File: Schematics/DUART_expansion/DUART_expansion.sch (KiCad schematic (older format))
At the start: 11 parts

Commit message: Initial working version (still unstable!)
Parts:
- added unit 5 of U1
- added unit 6 of U1
- added unit 4 of U2
- U1: renamed from U?; value 74AHC04 -> 74HC04; symbol 74xx:74AHC04 -> 74xx:74HC04
- gave numbers to parts that had none: 4
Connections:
- net +5V: now also U1.14 (VCC), U2.14 (VCC); no longer U1.7 (GND), U2.7 (GND)
- net CLK: now also U2.13
- net DUART_CEN: now also U2.11; no longer U2.8
- net GND: now also U1.7 (GND), U2.7 (GND), U1.13; no longer U1.14 (VCC), U2.14 (VCC)
- net d6: no longer U3.21 (D7)
- net d7: now also U3.21 (D7)
- new net: U1.10, U2.12
- new net: U1.11, U2.8
- no-connect marks 20 -> 21
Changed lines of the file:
@@
 $EndDescr
 $Comp
-L Connector_Generic:Conn_02x16_Odd_Even J?
+L Connector_Generic:Conn_02x16_Odd_Even J1
 U 1 1 5F15BD0D
 P 1400 1650
-F 0 "J?" H 1450 2567 50  0000 C CNN
+F 0 "J1" H 1450 2567 50  0000 C CNN
 F 1 "Expansion bus" H 1450 2476 50  0000 C CNN
 F 2 "" H 1400 1650 50  0001 C CNN
@@
 	3550 1850 3550 1750
 $Comp
-L Oscillator:CXO_DIP8 X?
+L Oscillator:CXO_DIP8 X1
 U 1 1 5F1792E7
 P 3550 1450
-F 0 "X?" H 3894 1496 50  0000 L CNN
+F 0 "X1" H 3894 1496 50  0000 L CNN
 F 1 "CXO_DIP8" H 3894 1405 50  0000 L CNN
 F 2 "Oscillator:Oscillator_DIP-8" H 4000 1100 50  0001 C CNN
@@
 	3850 1450 4300 1450
 $Comp
-L 74xx:74AHC04 U?
+L 74xx:74HC04 U1
 U 7 1 5F17BEEB
 P 1100 3800
-F 0 "U?" H 1330 3846 50  0000 L CNN
-F 1 "74AHC04" H 1330 3755 50  0000 L CNN
+F 0 "U1" H 1330 3846 50  0000 L CNN
+F 1 "74HC04" H 1330 3755 50  0000 L CNN
 F 2 "" H 1100 3800 50  0001 C CNN
 F 3 "https://assets.nexperia.com/documents/data-sheet/74AHC_AHCT04.pdf" H 1100 3800 50  0001 C CNN
@@
 	1    0    0    -1
 $EndComp
-Text GLabel 1100 3200 1    50   Input ~ 0
-GND
 Wire Wire Line
 	1100 3200 1100 3300
-Text GLabel 1100 4400 3    50   Input ~ 0
-+5V
 Wire Wire Line
 	1100 4400 1100 4300
 $Comp
-L 74xx:74AHC04 U?
+L 74xx:74HC04 U1
 U 1 1 5F17F7FF
 P 3500 2700
-F 0 "U?" H 3500 3017 50  0000 C CNN
-F 1 "74AHC04" H 3500 2926 50  0000 C CNN
+F 0 "U1" H 3500 3017 50  0000 C CNN
+F 1 "74HC04" H 3500 2926 50  0000 C CNN
 F 2 "" H 3500 2700 50  0001 C CNN
 F 3 "https://assets.nexperia.com/documents/data-sheet/74AHC_AHCT04.pdf" H 3500 2700 50  0001 C CNN
@@
 	3800 2700 3900 2700
 $Comp
-L 74xx:74AHC04 U?
+L 74xx:74HC04 U1
 U 2 1 5F185D8B
 P 3500 3900
-F 0 "U?" H 3500 4217 50  0000 C CNN
-F 1 "74AHC04" H 3500 4126 50  0000 C CNN
+F 0 "U1" H 3500 4217 50  0000 C CNN
+F 1 "74HC04" H 3500 4126 50  0000 C CNN
 F 2 "" H 3500 3900 50  0001 C CNN
 F 3 "https://assets.nexperia.com/documents/data-sheet/74AHC_AHCT04.pdf" H 3500 3900 50  0001 C CNN
@@
 $EndComp
 $Comp
-L 74xx:74HC00 U?
+L 74xx:74HC00 U2
 U 1 1 5F187D21
 P 3500 3250
-F 0 "U?" H 3500 3575 50  0000 C CNN
+F 0 "U2" H 3500 3575 50  0000 C CNN
 F 1 "74HC00" H 3500 3484 50  0000 C CNN
 F 2 "" H 3500 3250 50  0001 C CNN
@@
 	3100 3350 3200 3350
 $Comp
-L 74xx:74HC00 U?
+L 74xx:74HC00 U2
 U 5 1 5F18B90B
 P 1950 3800
-F 0 "U?" H 2180 3846 50  0000 L CNN
+F 0 "U2" H 2180 3846 50  0000 L CNN
 F 1 "74HC00" H 2180 3755 50  0000 L CNN
 F 2 "" H 1950 3800 50  0001 C CNN
@@
 	1    0    0    -1
 $EndComp
-Text GLabel 1950 3200 1    50   Input ~ 0
-GND
 Wire Wire Line
 	1950 3200 1950 3300
-Text GLabel 1950 4400 3    50   Input ~ 0
-+5V
 Wire Wire Line
 	1950 4400 1950 4300
@@
 	3100 3900 3200 3900
 $Comp
-L 74xx:74HC00 U?
+L 74xx:74HC00 U2
 U 2 1 5F19297E
 P 4200 4000
-F 0 "U?" H 4200 4325 50  0000 C CNN
+F 0 "U2" H 4200 4325 50  0000 C CNN
 F 1 "74HC00" H 4200 4234 50  0000 C CNN
 F 2 "" H 4200 4000 50  0001 C CNN
@@
 	3100 4100 3900 4100
 $Comp
-L 74xx:74AHC04 U?
+L 74xx:74HC04 U1
 U 3 1 5F197B7F
 P 3500 4600
-F 0 "U?" H 3500 4917 50  0000 C CNN
-F 1 "74AHC04" H 3500 4826 50  0000 C CNN
+F 0 "U1" H 3500 4917 50  0000 C CNN
+F 1 "74HC04" H 3500 4826 50  0000 C CNN
 F 2 "" H 3500 4600 50  0001 C CNN
 F 3 "https://assets.nexperia.com/documents/data-sheet/74AHC_AHCT04.pdf" H 3500 4600 50  0001 C CNN
@@
 	3100 4600 3200 4600
 $Comp
-L 74xx:74HC00 U?
+L 74xx:74HC00 U2
 U 3 1 5F199FB8
 P 4200 4700
-F 0 "U?" H 4200 5025 50  0000 C CNN
+F 0 "U2" H 4200 5025 50  0000 C CNN
 F 1 "74HC00" H 4200 4934 50  0000 C CNN
 F 2 "" H 4200 4700 50  0001 C CNN
@@
 Wire Bus Line
 	3000 4900 3000 4950
-Text GLabel 4600 4700 2    50   Output ~ 0
+Text GLabel 6000 4800 2    50   Output ~ 0
 DUART_CEN
 Wire Wire Line
 	4500 4700 4600 4700
 $Comp
-L DUART:SC26C92 U?
+L DUART:SC26C92 U3
 U 1 1 5F1A2B31
 P 6500 2400
-F 0 "U?" H 6450 2500 50  0000 L CNN
+F 0 "U3" H 6450 2500 50  0000 L CNN
 F 1 "SC26C92" H 6500 2300 50  0000 C CNN
 F 2 "" H 6500 2400 50  0001 C CNN
@@
 d5
 Text Label 6300 3300 1    50   ~ 0
-d6
+d7
 Wire Wire Line
 	6000 3200 6000 3300
@@
 Wire Wire Line
 	7400 2500 7300 2500
+Text GLabel 1100 4400 3    50   Input ~ 0
+GND
+Text GLabel 1950 4400 3    50   Input ~ 0
+GND
+Text GLabel 1100 3200 1    50   Input ~ 0
++5V
+Text GLabel 1950 3200 1    50   Input ~ 0
++5V
+$Comp
+L 74xx:74HC04 U1
+U 5 1 5F188CDA
+P 4900 4700
+F 0 "U1" H 4900 5017 50  0000 C CNN
+F 1 "74HC04" H 4900 4926 50  0000 C CNN
+F 2 "" H 4900 4700 50  0001 C CNN
+F 3 "https://assets.nexperia.com/documents/data-sheet/74AHC_AHCT04.pdf" H 4900 4700 50  0001 C CNN
+	5    4900 4700
+	1    0    0    -1
+$EndComp
+$Comp
+L 74xx:74HC00 U2
+U 4 1 5F189A33
+P 5600 4800
+F 0 "U2" H 5600 5125 50  0000 C CNN
+F 1 "74HC00" H 5600 5034 50  0000 C CNN
+F 2 "" H 5600 4800 50  0001 C CNN
+F 3 "http://www.ti.com/lit/gpn/sn74hc00" H 5600 4800 50  0001 C CNN
+	4    5600 4800
+	1    0    0    -1
+$EndComp
+Wire Wire Line
+	5200 4700 5300 4700
+Text GLabel 3100 5050 0    50   Input ~ 0
+CLK
+Wire Wire Line
+	3100 5050 5200 5050
+Wire Wire Line
+	5200 5050 5200 4900
+Wire Wire Line
+	5200 4900 5300 4900
+Wire Wire Line
+	5900 4800 6000 4800
+$Comp
+L 74xx:74HC04 U1
+U 6 1 5F19385D
+P 1500 5100
+F 0 "U1" H 1500 5417 50  0000 C CNN
+F 1 "74HC04" H 1500 5326 50  0000 C CNN
+F 2 "" H 1500 5100 50  0001 C CNN
+F 3 "https://assets.nexperia.com/documents/data-sheet/74AHC_AHCT04.pdf" H 1500 5100 50  0001 C CNN
+	6    1500 5100
+	1    0    0    -1
+$EndComp
+Text GLabel 1100 5100 0    50   Input ~ 0
+GND
+Wire Wire Line
+	1100 5100 1200 5100
+NoConn ~ 1800 5100
 Wire Bus Line
 	5500 1400 6300 1400

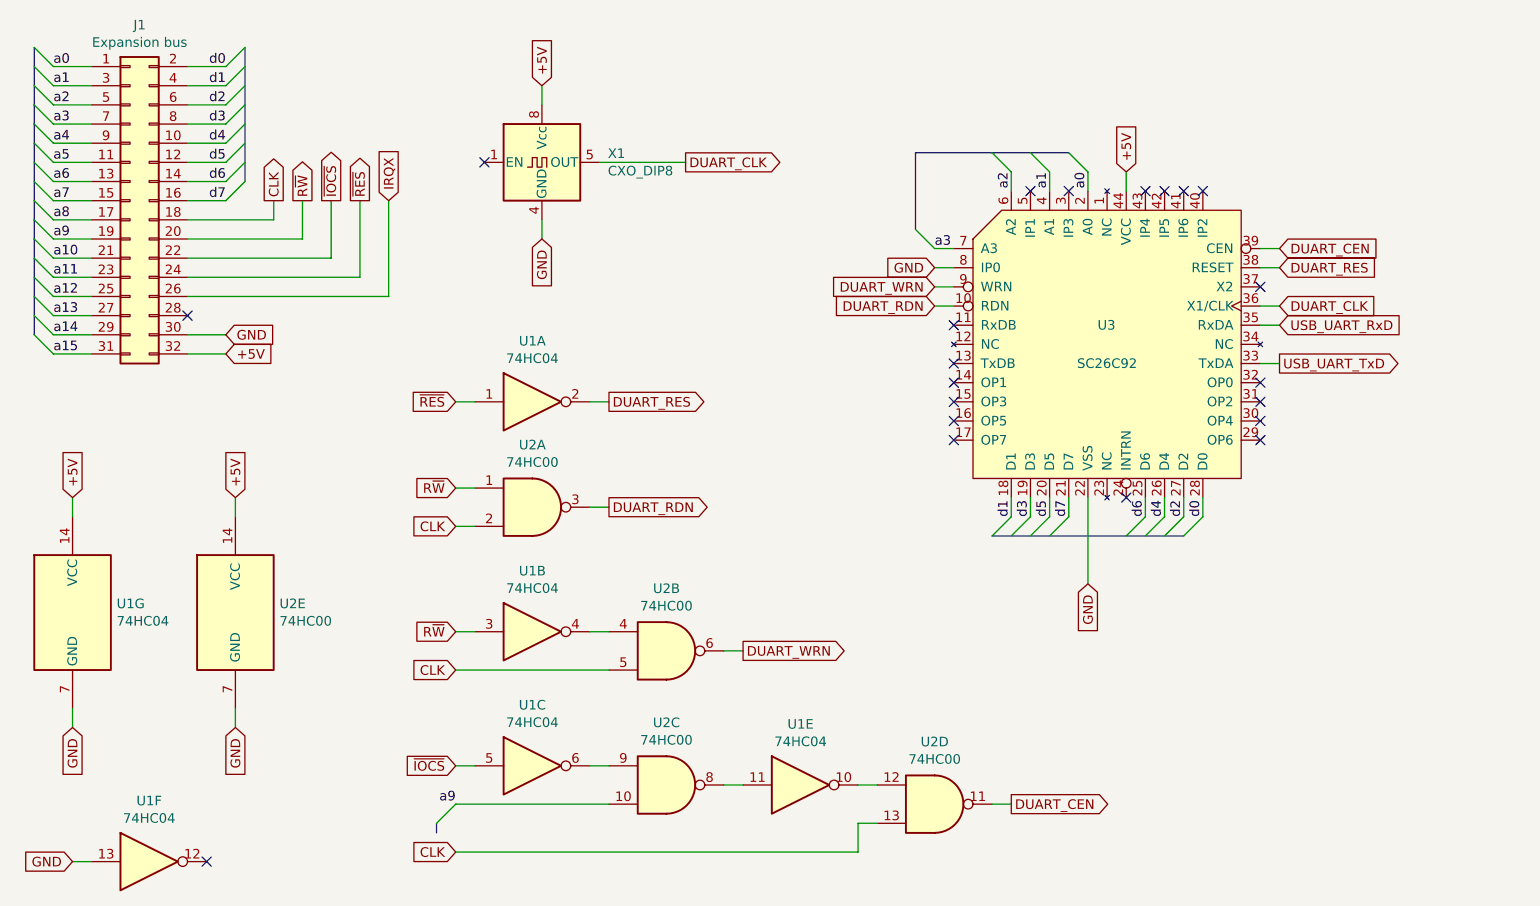
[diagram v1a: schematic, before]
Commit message: Replaced can with crystal, removed unused connections
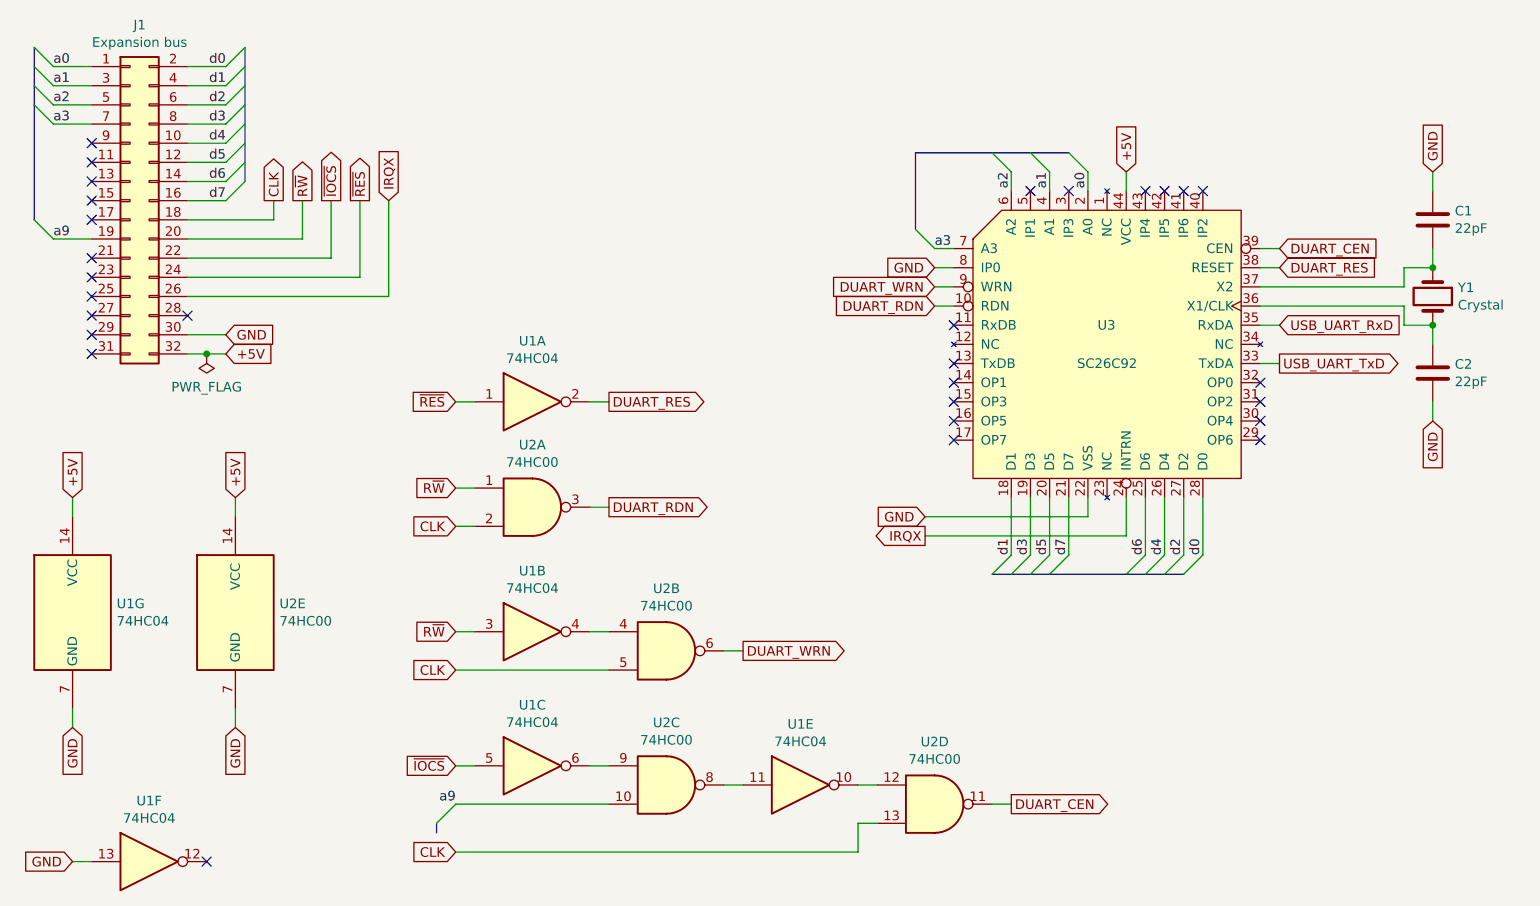
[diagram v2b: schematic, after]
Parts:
- removed X1: CXO_DIP8, Oscillator:Oscillator_DIP-8, symbol Oscillator:CXO_DIP8
- added C1, C2: 22pF, symbol Device:C
- added Y1: Crystal, symbol Device:Crystal
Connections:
- net GND: now also C1.1, C2.2
- net IRQX: now also U3.24 (INTRN)
- net at U3.37 (X2): now also C1.2, Y1.1
- net DUART_CLK: no longer names the net of U3.36 (X1/CLK)
- net DUART_CLK: now also C2.1, Y1.2
- net a10: no longer names the net of J1.21 (Pin_21)
- net a11: no longer names the net of J1.23 (Pin_23)
- net a12: no longer names the net of J1.25 (Pin_25)
- net a13: no longer names the net of J1.27 (Pin_27)
- net a14: no longer names the net of J1.29 (Pin_29)
- net a15: no longer names the net of J1.31 (Pin_31)
- net a4: no longer names the net of J1.9 (Pin_9)
- net a5: no longer names the net of J1.11 (Pin_11)
- net a6: no longer names the net of J1.13 (Pin_13)
- net a7: no longer names the net of J1.15 (Pin_15)
- net a8: no longer names the net of J1.17 (Pin_17)
- no-connect marks 21 -> 29
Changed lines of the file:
@@
 Text Label 1000 1850 0    50   ~ 0
 a9
-Text Label 1000 1350 0    50   ~ 0
-a4
-Text Label 1000 1450 0    50   ~ 0
-a5
-Text Label 1000 1550 0    50   ~ 0
-a6
-Text Label 1000 1650 0    50   ~ 0
-a7
-Text Label 1000 1750 0    50   ~ 0
-a8
-Text Label 1000 1950 0    50   ~ 0
-a10
-Text Label 1000 2050 0    50   ~ 0
-a11
-Text Label 1000 2150 0    50   ~ 0
-a12
-Text Label 1000 2250 0    50   ~ 0
-a13
-Text Label 1000 2350 0    50   ~ 0
-a14
-Text Label 1000 2450 0    50   ~ 0
-a15
-Wire Wire Line
-	1000 1350 1200 1350
-Wire Wire Line
-	1000 1450 1200 1450
-Wire Wire Line
-	1000 1550 1200 1550
-Wire Wire Line
-	1000 1650 1200 1650
-Wire Wire Line
-	1000 1750 1200 1750
 Wire Wire Line
 	1000 1850 1200 1850
-Wire Wire Line
-	1000 1950 1200 1950
-Wire Wire Line
-	1000 2050 1200 2050
-Wire Wire Line
-	1000 2150 1200 2150
-Wire Wire Line
-	1000 2250 1200 2250
-Wire Wire Line
-	1000 2350 1200 2350
-Wire Wire Line
-	1000 2450 1200 2450
-Entry Wire Line
-	900  1250 1000 1350
-Entry Wire Line
-	900  1350 1000 1450
-Entry Wire Line
-	900  1450 1000 1550
-Entry Wire Line
-	900  1550 1000 1650
-Entry Wire Line
-	900  1650 1000 1750
 Entry Wire Line
 	900  1750 1000 1850
-Entry Wire Line
-	900  1850 1000 1950
-Entry Wire Line
-	900  1950 1000 2050
-Entry Wire Line
-	900  2050 1000 2150
-Entry Wire Line
-	900  2150 1000 2250
-Entry Wire Line
-	900  2250 1000 2350
-Entry Wire Line
-	900  2350 1000 2450
 Text GLabel 1900 2350 2    50   Input ~ 0
 GND
@@
 +5V
 Wire Wire Line
-	1900 2450 1700 2450
+	1900 2450 1800 2450
 Wire Wire Line
 	1700 2350 1900 2350
@@
 Wire Wire Line
 	2750 2150 1700 2150
-Text GLabel 3550 1850 3    50   Input ~ 0
-GND
-Wire Wire Line
-	3550 1850 3550 1750
-$Comp
-L Oscillator:CXO_DIP8 X1
-U 1 1 5F1792E7
-P 3550 1450
-F 0 "X1" H 3894 1496 50  0000 L CNN
-F 1 "CXO_DIP8" H 3894 1405 50  0000 L CNN
-F 2 "Oscillator:Oscillator_DIP-8" H 4000 1100 50  0001 C CNN
-F 3 "http://cdn-reichelt.de/documents/datenblatt/B400/OSZI.pdf" H 3450 1450 50  0001 C CNN
-	1    3550 1450
-	1    0    0    -1
-$EndComp
-Text GLabel 3550 1050 1    50   Input ~ 0
-+5V
-Wire Wire Line
-	3550 1050 3550 1150
-NoConn ~ 3250 1450
-Text GLabel 4300 1450 2    50   Output ~ 0
-DUART_CLK
-Wire Wire Line
-	3850 1450 4300 1450
 $Comp
 L 74xx:74HC04 U1
@@
 Wire Wire Line
 	4500 4700 4600 4700
-$Comp
-L DUART:SC26C92 U3
-U 1 1 5F1A2B31
-P 6500 2400
-F 0 "U3" H 6450 2500 50  0000 L CNN
-F 1 "SC26C92" H 6500 2300 50  0000 C CNN
-F 2 "" H 6500 2400 50  0001 C CNN
-F 3 "" H 6500 2400 50  0001 C CNN
-	1    6500 2400
-	1    0    0    -1
-$EndComp
-Text GLabel 6400 3650 3    50   Input ~ 0
-GND
-Wire Wire Line
-	6400 3650 6400 3200
+Text GLabel 5550 3300 0    50   Input ~ 0
+GND
 Text GLabel 6600 1500 1    50   Input ~ 0
 +5V
@@
 Wire Wire Line
 	7400 2000 7300 2000
-Text GLabel 7400 2200 2    50   Input ~ 0
-DUART_CLK
-Wire Wire Line
-	7400 2200 7300 2200
-NoConn ~ 7300 2100
 Text GLabel 7400 1900 2    50   Input ~ 0
 DUART_CEN
@@
 NoConn ~ 5700 2700
 NoConn ~ 5700 2600
-NoConn ~ 6600 3200
 NoConn ~ 5700 2300
 NoConn ~ 5700 2500
-Text Label 7000 3300 1    50   ~ 0
+Text Label 7000 3500 1    50   ~ 0
 d0
-Text Label 6900 3300 1    50   ~ 0
+Text Label 6900 3500 1    50   ~ 0
 d2
-Text Label 6800 3300 1    50   ~ 0
+Text Label 6800 3500 1    50   ~ 0
 d4
-Text Label 6700 3300 1    50   ~ 0
+Text Label 6700 3500 1    50   ~ 0
 d6
-Text Label 6000 3300 1    50   ~ 0
+Text Label 6000 3500 1    50   ~ 0
 d1
-Text Label 6100 3300 1    50   ~ 0
+Text Label 6100 3500 1    50   ~ 0
 d3
-Text Label 6200 3300 1    50   ~ 0
+Text Label 6200 3500 1    50   ~ 0
 d5
-Text Label 6300 3300 1    50   ~ 0
+Text Label 6300 3500 1    50   ~ 0
 d7
 Wire Wire Line
-	6000 3200 6000 3300
-Wire Wire Line
-	6100 3200 6100 3300
-Wire Wire Line
-	6200 3200 6200 3300
-Wire Wire Line
-	6300 3200 6300 3300
-Wire Wire Line
-	6700 3200 6700 3300
-Wire Wire Line
-	6800 3200 6800 3300
-Wire Wire Line
-	6900 3200 6900 3300
-Wire Wire Line
-	7000 3200 7000 3300
-Entry Wire Line
-	5900 3400 6000 3300
-Entry Wire Line
-	6000 3400 6100 3300
-Entry Wire Line
-	6100 3400 6200 3300
-Entry Wire Line
-	6200 3400 6300 3300
-Entry Wire Line
-	6600 3400 6700 3300
-Entry Wire Line
-	6700 3400 6800 3300
-Entry Wire Line
-	6800 3400 6900 3300
-Entry Wire Line
-	6900 3400 7000 3300
+	6000 3200 6000 3500
+Wire Wire Line
+	6100 3200 6100 3500
+Wire Wire Line
+	6200 3200 6200 3500
+Wire Wire Line
+	6300 3200 6300 3500
+Wire Wire Line
+	6700 3200 6700 3500
+Wire Wire Line
+	6800 3200 6800 3500
+Wire Wire Line
+	6900 3200 6900 3500
+Wire Wire Line
+	7000 3200 7000 3500
+Entry Wire Line
+	5900 3600 6000 3500
+Entry Wire Line
+	6000 3600 6100 3500
+Entry Wire Line
+	6100 3600 6200 3500
+Entry Wire Line
+	6200 3600 6300 3500
+Entry Wire Line
+	6600 3600 6700 3500
+Entry Wire Line
+	6700 3600 6800 3500
+Entry Wire Line
+	6800 3600 6900 3500
+Entry Wire Line
+	6900 3600 7000 3500
 Text GLabel 7400 2500 2    50   Output ~ 0
 USB_UART_TxD
@@
 	1100 5100 1200 5100
 NoConn ~ 1800 5100
+Text GLabel 5550 3400 0    50   Output ~ 0
+IRQX
+Wire Wire Line
+	5550 3400 6600 3400
+Wire Wire Line
+	6600 3400 6600 3200
+Wire Wire Line
+	5550 3300 6400 3300
+Wire Wire Line
+	6400 3300 6400 3200
+$Comp
+L DUART:SC26C92 U3
+U 1 1 5F1A2B31
+P 6500 2400
+F 0 "U3" H 6450 2500 50  0000 L CNN
+F 1 "SC26C92" H 6500 2300 50  0000 C CNN
+F 2 "" H 6500 2400 50  0001 C CNN
+F 3 "" H 6500 2400 50  0001 C CNN
+	1    6500 2400
+	1    0    0    -1
+$EndComp
+$Comp
+L Device:Crystal Y1
+U 1 1 5F1DF768
+P 8200 2150
+F 0 "Y1" V 8154 2281 50  0000 L CNN
+F 1 "Crystal" V 8245 2281 50  0000 L CNN
+F 2 "" H 8200 2150 50  0001 C CNN
+F 3 "~" H 8200 2150 50  0001 C CNN
+	1    8200 2150
+	0    1    1    0
+$EndComp
+Wire Wire Line
+	7300 2100 8050 2100
+Wire Wire Line
+	8050 2100 8050 2000
+Wire Wire Line
+	8050 2000 8200 2000
+Wire Wire Line
+	7300 2200 8050 2200
+Wire Wire Line
+	8050 2200 8050 2300
+Wire Wire Line
+	8050 2300 8200 2300
+Wire Wire Line
+	8200 2400 8200 2300
+Connection ~ 8200 2300
+Wire Wire Line
+	8200 2000 8200 1900
+Connection ~ 8200 2000
+$Comp
+L Device:C C1
+U 1 1 5F1EB8DE
+P 8200 1750
+F 0 "C1" H 8315 1796 50  0000 L CNN
+F 1 "22pF" H 8315 1705 50  0000 L CNN
+F 2 "" H 8238 1600 50  0001 C CNN
+F 3 "~" H 8200 1750 50  0001 C CNN
+	1    8200 1750
+	1    0    0    -1
+$EndComp
+$Comp
+L Device:C C2
+U 1 1 5F1EC246
+P 8200 2550
+F 0 "C2" H 8315 2596 50  0000 L CNN
+F 1 "22pF" H 8315 2505 50  0000 L CNN
+F 2 "" H 8238 2400 50  0001 C CNN
+F 3 "~" H 8200 2550 50  0001 C CNN
+	1    8200 2550
+	1    0    0    -1
+$EndComp
+Text GLabel 8200 1500 1    50   Input ~ 0
+GND
+Text GLabel 8200 2800 3    50   Input ~ 0
+GND
+Wire Wire Line
+	8200 2800 8200 2700
+Wire Wire Line
+	8200 1600 8200 1500
+$Comp
+L power:PWR_FLAG #FLG0101
+U 1 1 5F1F24E0
+P 1800 2450
+F 0 "#FLG0101" H 1800 2525 50  0001 C CNN
+F 1 "PWR_FLAG" H 1800 2623 50  0000 C CNN
+F 2 "" H 1800 2450 50  0001 C CNN
+F 3 "~" H 1800 2450 50  0001 C CNN
+	1    1800 2450
+	-1   0    0    1
+$EndComp
+Connection ~ 1800 2450
+Wire Wire Line
+	1800 2450 1700 2450
+NoConn ~ 1200 1350
+NoConn ~ 1200 1450
+NoConn ~ 1200 1550
+NoConn ~ 1200 1650
+NoConn ~ 1200 1750
+NoConn ~ 1200 1950
+NoConn ~ 1200 2050
+NoConn ~ 1200 2150
+NoConn ~ 1200 2250
+NoConn ~ 1200 2350
+NoConn ~ 1200 2450
 Wire Bus Line
 	5500 1400 6300 1400
 Wire Bus Line
+	900  850  900  1750
+Wire Bus Line
 	2000 850  2000 1550
 Wire Bus Line
-	5900 3400 6900 3400
-Wire Bus Line
-	900  850  900  2350
+	5900 3600 6900 3600
 $EndSCHEMATC
